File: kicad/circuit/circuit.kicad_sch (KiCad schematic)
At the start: 15 parts, among them J1.1 Digital, J1.2 Analog, J2 Handbrake, J3 Encoder, J4 Joystick, J5 Pedals, J6 RJ45, J7.1.1 LCD Socket, J7.1.2 PCF8574 LCD Socekt, J7.2 PCF8574 I²C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

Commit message: remove lcd and add gitignore for kicad
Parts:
- removed J7.1.1: LCD Socket, Connector_PinSocket_2.54mm:PinSocket_1x16_P2.54mm_Vertical_SMD_Pin1Left, symbol Connector:Conn_01x16_Socket
- removed J7.1.2: PCF8574 LCD Socekt, Connector_PinSocket_2.54mm:PinSocket_1x16_P2.54mm_Vertical_SMD_Pin1Left, symbol Connector:Conn_01x16_Socket
- removed SW1: Reset, Button_Switch_SMD:SW_Push_1P1T_NO_6x6mm_H9.5mm, symbol Switch:SW_Push
- removed U1: LCD-016N002L, symbol Display_Character:LCD-016N002L
- added R3, R4: 4.7k, Resistor_SMD:R_0402_1005Metric, symbol Device:R
- J2: renamed from J5; footprint Connector_PinHeader_2.54mm:PinHeader_1x05_P2.54mm_Vertical_SMD_Pin1Left -> Connector_PinHeader_2.54mm:PinHeader_2x03_P2.54mm_Vertical_SMD
- J3: renamed from J4; footprint Connector_PinHeader_2.54mm:PinHeader_1x05_P2.54mm_Vertical_SMD_Pin1Left -> Connector_PinHeader_2.54mm:PinHeader_2x03_P2.54mm_Vertical_SMD
- J4: renamed from J3; footprint Connector_PinHeader_2.54mm:PinHeader_1x05_P2.54mm_Vertical_SMD_Pin1Left -> Connector_PinHeader_2.54mm:PinHeader_2x03_P2.54mm_Vertical_SMD
- J5: renamed from J2; footprint Connector_PinHeader_2.54mm:PinHeader_1x03_P2.54mm_Vertical_SMD_Pin1Left -> Connector_PinHeader_2.54mm:PinHeader_2x02_P2.54mm_Vertical_SMD
- J6: renamed from J7.2; footprint Connector_PinHeader_2.54mm:PinHeader_1x04_P2.54mm_Vertical_SMD_Pin1Left -> Connector_PinHeader_2.54mm:PinHeader_2x02_P2.54mm_Vertical_SMD
- R1: renamed from R2; footprint Resistor_SMD:R_0805_2012Metric_Pad1.20x1.40mm_HandSolder -> Resistor_SMD:R_0402_1005Metric
- R2: renamed from R1; footprint Resistor_SMD:R_0805_2012Metric_Pad1.20x1.40mm_HandSolder -> Resistor_SMD:R_0402_1005Metric
- renumbered J8 to J7, J6 to J8
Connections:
- net *D3/SCL: now also R4.2
- net +5V: now also R3.1, R4.1
- net D2/SDA: now also R3.2
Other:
- moved on the sheet: J4, J7, J8, R1, R2

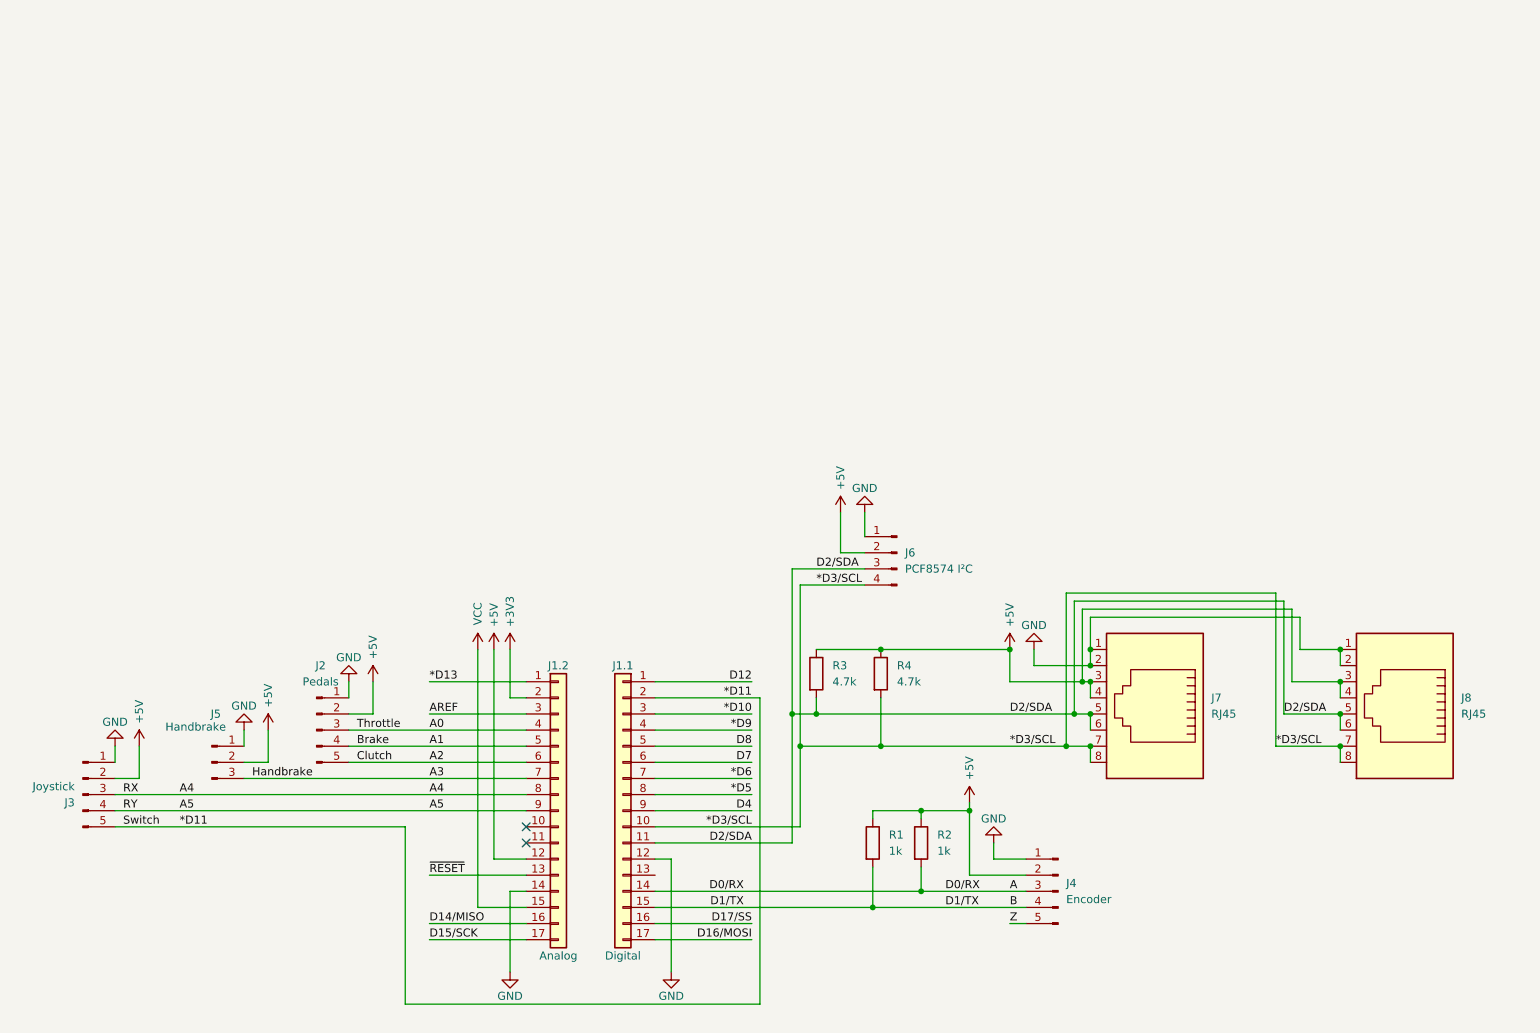
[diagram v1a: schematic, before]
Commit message: add ps4 joystick pcb + data over rj45
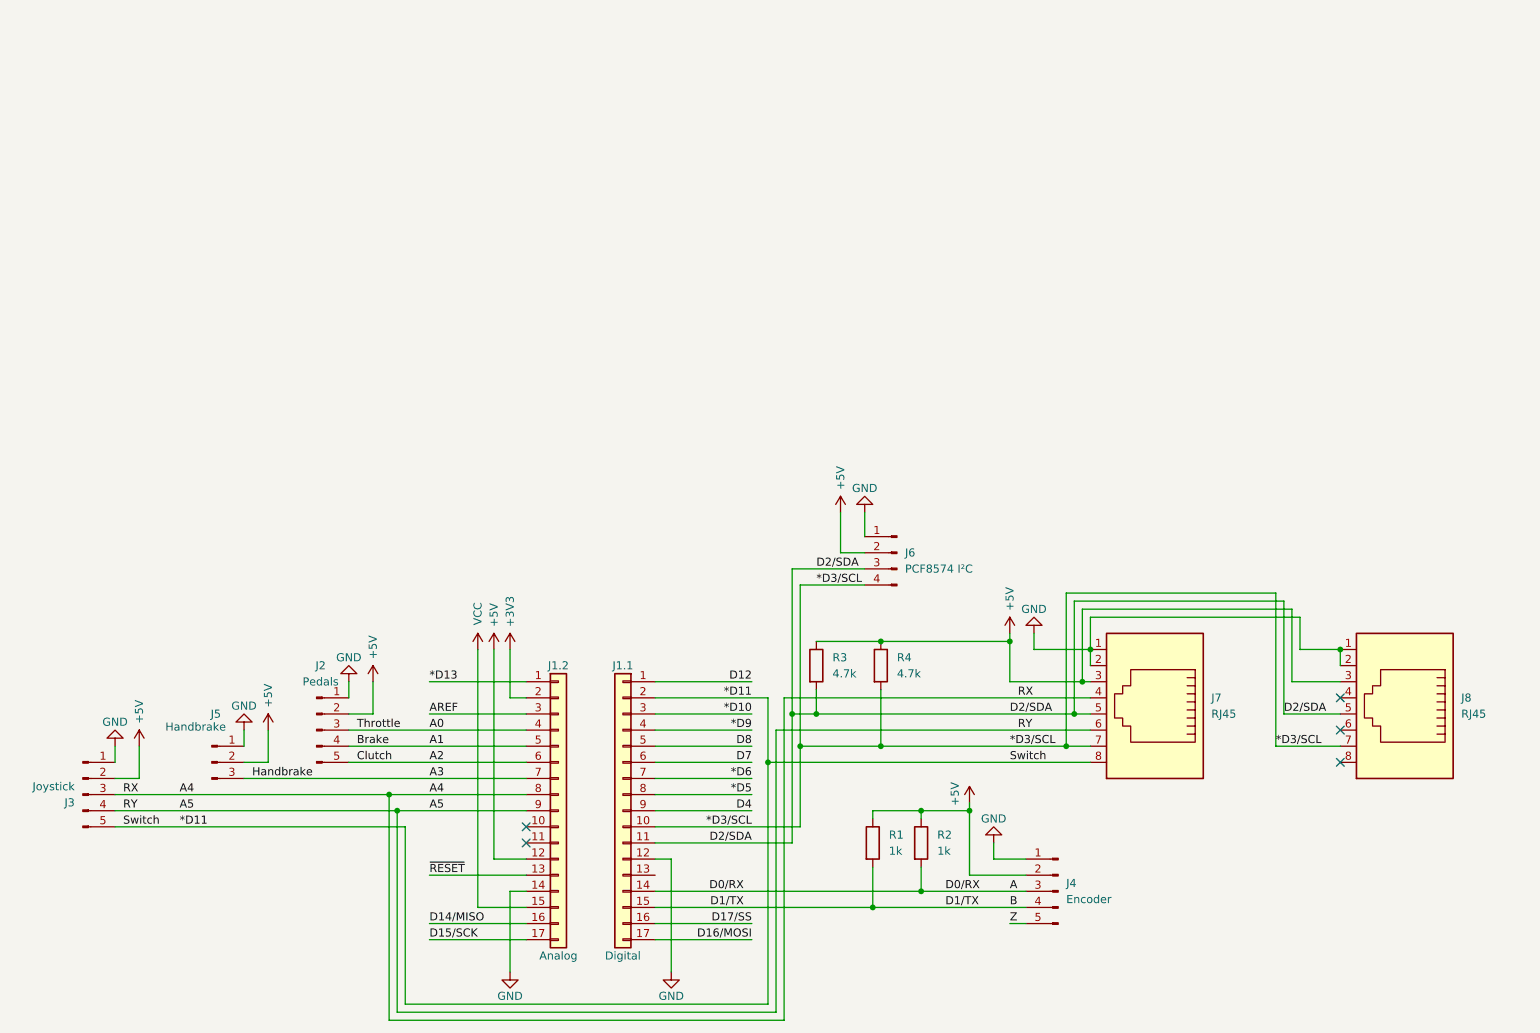
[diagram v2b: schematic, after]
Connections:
- net *D11: now also J7.8
- net *D3/SCL: no longer J7.8, J8.8
- net +5V: no longer J7.4, J8.4
- net A4: now also J7.4
- net A5: now also J7.6
- net D2/SDA: no longer J7.6, J8.6
- no-connect marks 2 -> 5
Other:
- moved on the sheet: R3, R4

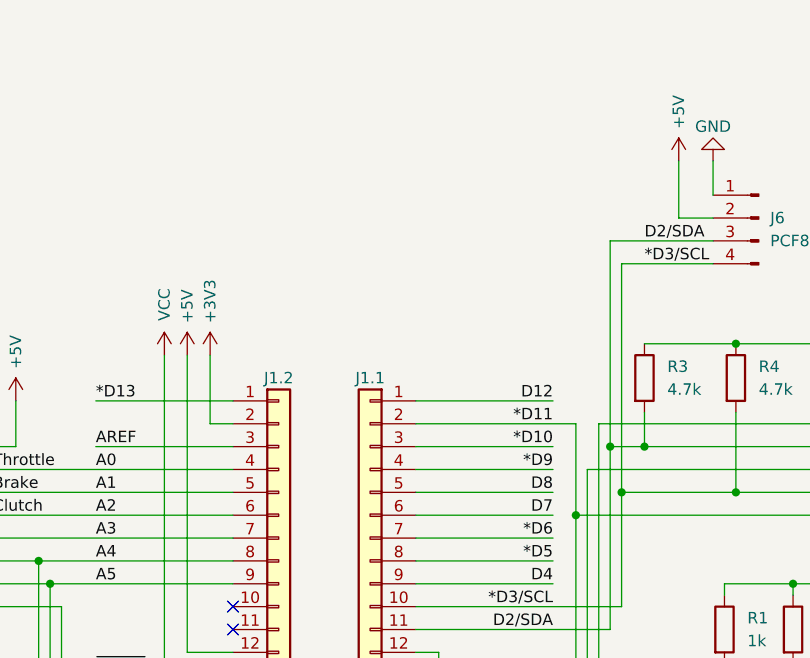
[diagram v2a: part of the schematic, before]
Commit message: add force feedback device to layout
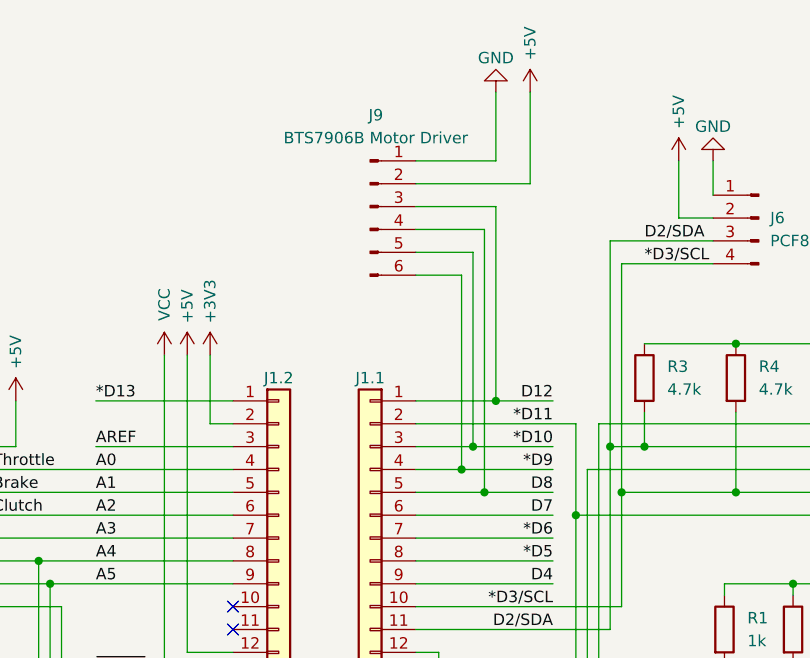
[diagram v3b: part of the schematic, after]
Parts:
- added J9: BTS7906B Motor Driver, Connector_PinHeader_2.54mm:PinHeader_2x03_P2.54mm_Vertical_SMD, symbol Connector:Conn_01x06_Pin
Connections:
- net *D10: now also J9.5 (Pin_5)
- net *D9: now also J9.6 (Pin_6)
- net +5V: now also J9.2 (Pin_2)
- net D12: now also J9.3 (Pin_3)
- net D8: now also J9.4 (Pin_4)
- net GND: now also J9.1 (Pin_1)

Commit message: update release v1.0.0
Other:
- company: (none) -> https://github.com/lusmdl
- title: (none) -> Arduino Micro Board
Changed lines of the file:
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@@
 	(paper "A4")
 	(title_block
-		(date "sam. 04 avril 2015")
+		(title "Arduino Micro Board")
+		(date "2025-01-14")
+		(rev "v1.0.0")
+		(company "https://github.com/lusmdl")
 	)
 	(junction
